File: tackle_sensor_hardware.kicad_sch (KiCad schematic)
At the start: 38 parts, among them J1 Conn_01x02_Male, J2 Conn_01x04_Male, J3 Conn_01x02_Male, Q1 DMP4051LK3, Q2 2N7002K, Q3 2N7002K, Q4 2N7002K, T1 DRQ125-330-R, U1 LIS2DE12, U2 STM32G031Fx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

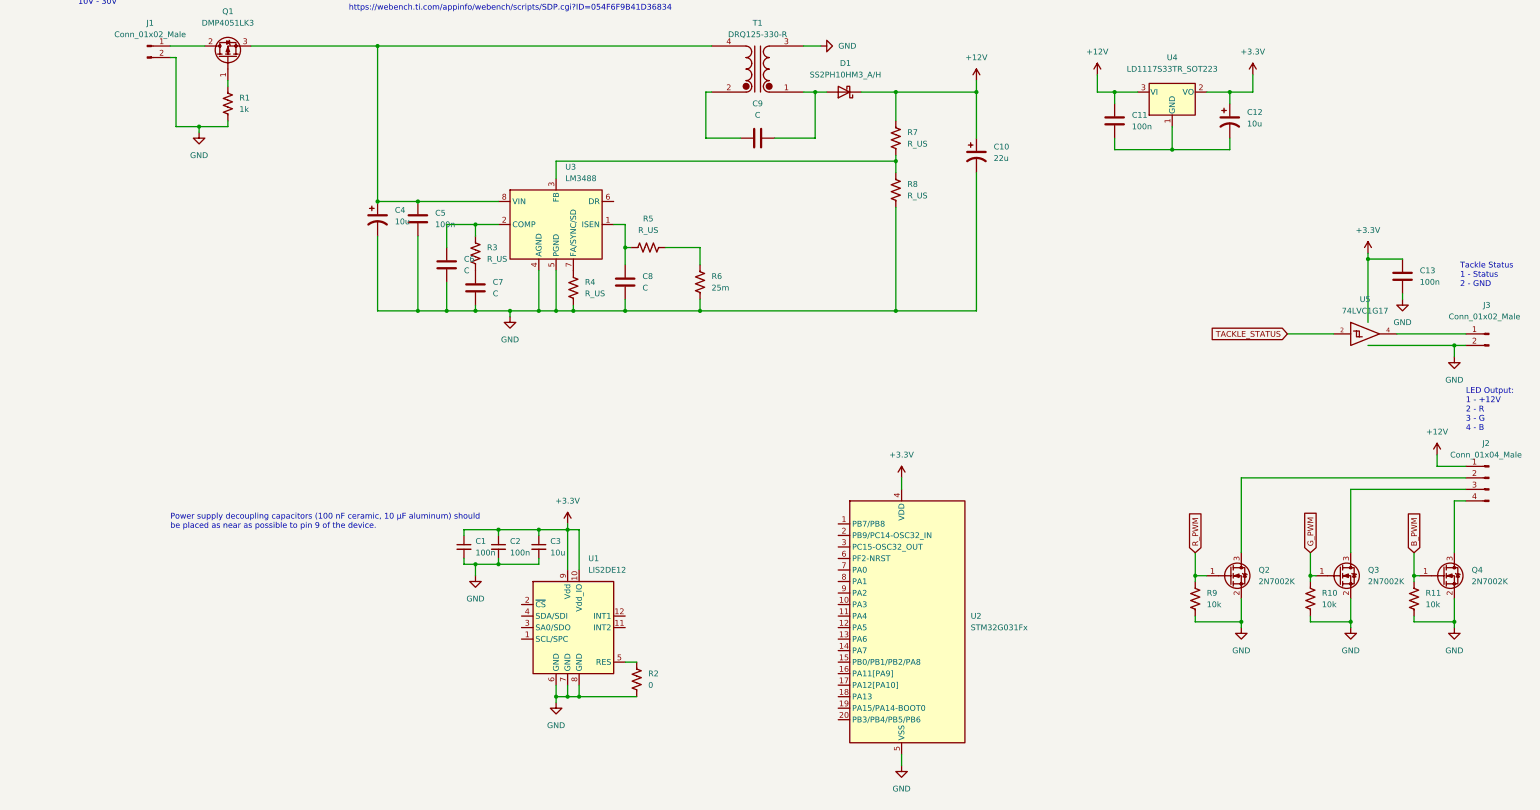
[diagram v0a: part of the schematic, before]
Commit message: (WIP) added prog header to schematic and added some WIP notes.
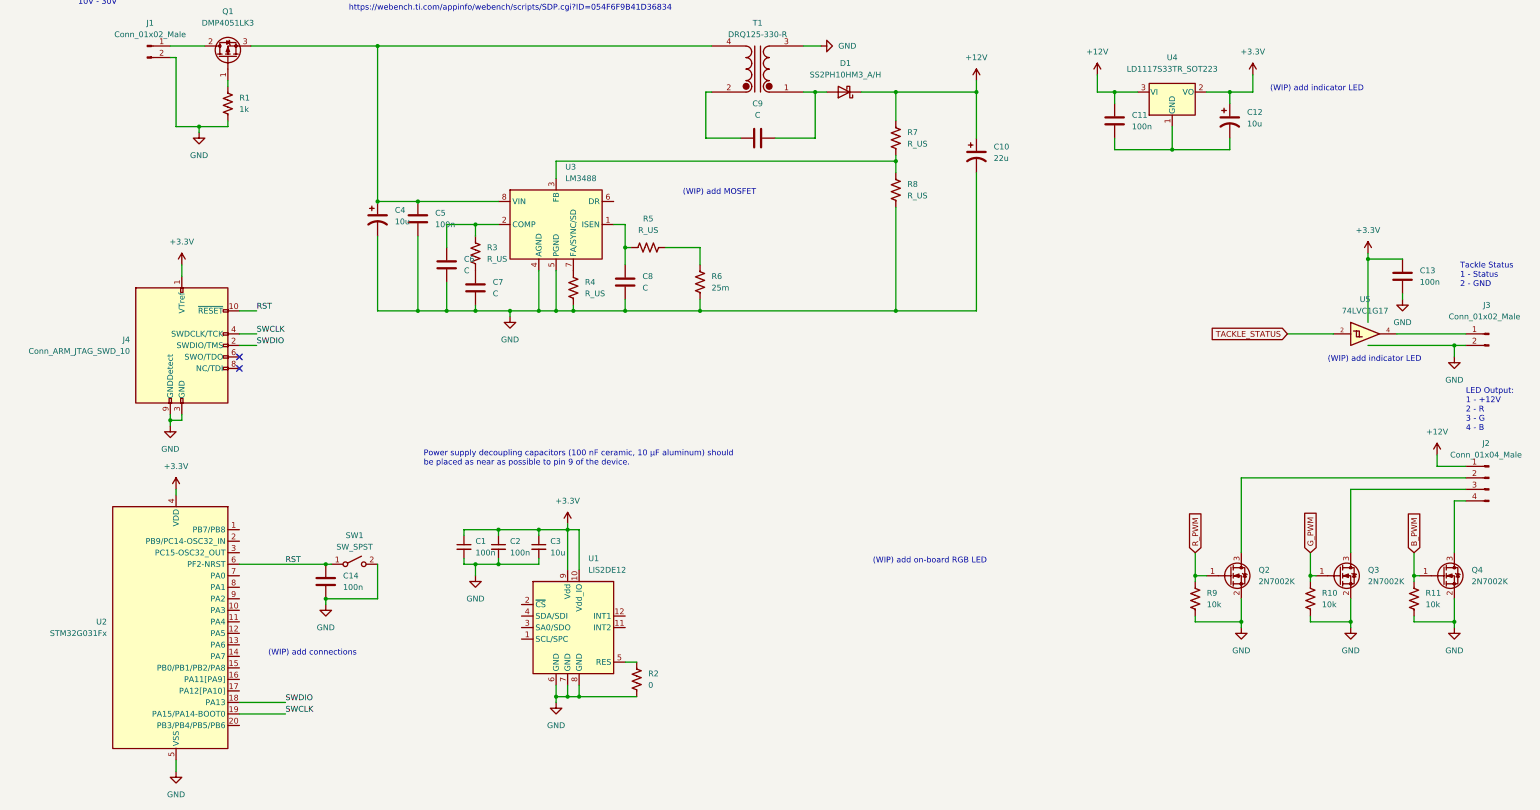
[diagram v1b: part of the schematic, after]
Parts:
- added C14: 100n, symbol Device:C
- added J4: Conn_ARM_JTAG_SWD_10, Connector_PinHeader_1.27mm:PinHeader_2x05_P1.27mm_Vertical, symbol Connector:Conn_ARM_JTAG_SWD_10
- added SW1: SW_SPST, symbol Switch:SW_SPST
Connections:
- net +3V3: now also J4.1 (VTref)
- net GND: now also C14.2, J4.3 (GND), J4.5 (GND), J4.9 (GNDDetect), SW1.2 (B)
- net SWDIO: now reaches U2.18 (PA13)
- net SWDIO: now also J4.2 (SWDIO/TMS)
- net SWCLK: now reaches U2.19 (PA15/PA14-BOOT0)
- net SWCLK: now also J4.4 (SWDCLK/TCK)
- net RST: now reaches U2.6 (PF2-NRST)
- net RST: now also C14.1, J4.10 (~{RESET}), SW1.1 (A)
- no-connect marks 0 -> 2
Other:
- note added: "(WIP) add MOSFET"
- note added: "(WIP) add connections"
- note added: "(WIP) add indicator LED"
- note added: "(WIP) add on-board RGB LED"
- moved on the sheet: U2

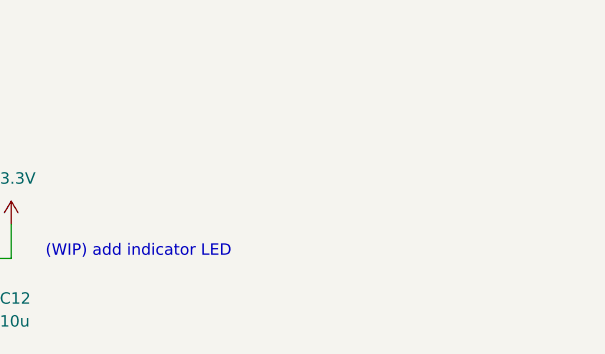
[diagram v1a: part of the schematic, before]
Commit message: added mounting holes
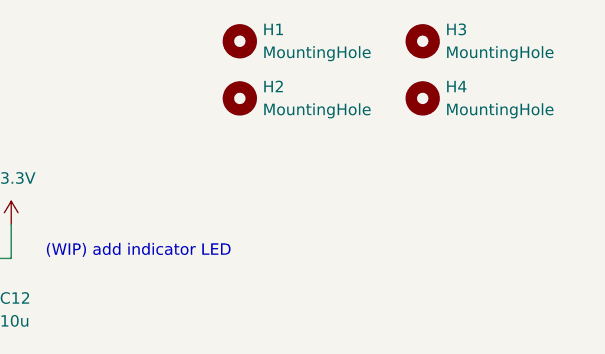
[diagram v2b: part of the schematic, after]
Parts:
- added H1, H2, H3, H4: MountingHole, MountingHole:MountingHole_3.2mm_M3, symbol Mechanical:MountingHole
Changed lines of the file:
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@@
     (pin "2")
+  )
+  (symbol (lib_id "Mechanical:MountingHole") (at 302.26 27.94 0) (unit 1)
+    (in_bom yes) (on_board yes) (fields_autoplaced)
+    (property "Reference" "H2" (id 0) (at 304.8 26.6699 0)
+      (effects (font (size 1.27 1.27)) (justify left))
+    )
+    (property "Value" "MountingHole" (id 1) (at 304.8 29.2099 0)
+      (effects (font (size 1.27 1.27)) (justify left))
+    )
+    (property "Footprint" "MountingHole:MountingHole_3.2mm_M3" (id 2) (at 302.26 27.94 0)
+      (effects (font (size 1.27 1.27)) hide)
+    )
+    (property "Datasheet" "~" (id 3) (at 302.26 27.94 0)
+      (effects (font (size 1.27 1.27)) hide)
+    )
   )
   (symbol (lib_id "Device:C") (at 105.41 88.9 0) (unit 1)
@@
     (pin "4")
   )
+  (symbol (lib_id "Mechanical:MountingHole") (at 322.58 21.59 0) (unit 1)
+    (in_bom yes) (on_board yes) (fields_autoplaced)
+    (property "Reference" "H3" (id 0) (at 325.12 20.3199 0)
+      (effects (font (size 1.27 1.27)) (justify left))
+    )
+    (property "Value" "MountingHole" (id 1) (at 325.12 22.8599 0)
+      (effects (font (size 1.27 1.27)) (justify left))
+    )
+    (property "Footprint" "MountingHole:MountingHole_3.2mm_M3" (id 2) (at 322.58 21.59 0)
+      (effects (font (size 1.27 1.27)) hide)
+    )
+    (property "Datasheet" "~" (id 3) (at 322.58 21.59 0)
+      (effects (font (size 1.27 1.27)) hide)
+    )
+  )
   (symbol (lib_id "Connector:Conn_ARM_JTAG_SWD_10") (at 40.64 101.6 0) (unit 1)
     (in_bom yes) (on_board yes) (fields_autoplaced)
@@
     (pin "2")
   )
+  (symbol (lib_id "Mechanical:MountingHole") (at 322.58 27.94 0) (unit 1)
+    (in_bom yes) (on_board yes) (fields_autoplaced)
+    (property "Reference" "H4" (id 0) (at 325.12 26.6699 0)
+      (effects (font (size 1.27 1.27)) (justify left))
+    )
+    (property "Value" "MountingHole" (id 1) (at 325.12 29.2099 0)
+      (effects (font (size 1.27 1.27)) (justify left))
+    )
+    (property "Footprint" "MountingHole:MountingHole_3.2mm_M3" (id 2) (at 322.58 27.94 0)
+      (effects (font (size 1.27 1.27)) hide)
+    )
+    (property "Datasheet" "~" (id 3) (at 322.58 27.94 0)
+      (effects (font (size 1.27 1.27)) hide)
+    )
+  )
+  (symbol (lib_id "Mechanical:MountingHole") (at 302.26 21.59 0) (unit 1)
+    (in_bom yes) (on_board yes) (fields_autoplaced)
+    (property "Reference" "H1" (id 0) (at 304.8 20.3199 0)
+      (effects (font (size 1.27 1.27)) (justify left))
+    )
+    (property "Value" "MountingHole" (id 1) (at 304.8 22.8599 0)
+      (effects (font (size 1.27 1.27)) (justify left))
+    )
+    (property "Footprint" "MountingHole:MountingHole_3.2mm_M3" (id 2) (at 302.26 21.59 0)
+      (effects (font (size 1.27 1.27)) hide)
+    )
+    (property "Datasheet" "~" (id 3) (at 302.26 21.59 0)
+      (effects (font (size 1.27 1.27)) hide)
+    )
+  )
   (symbol (lib_id "power:GND") (at 181.61 35.56 90) (unit 1)
     (in_bom yes) (on_board yes) (fields_autoplaced)
@@
       (reference "D1") (unit 1) (value "SS2PH10HM3_A/H") (footprint "")
     )
+    (path "/dff5c17e-362e-4954-b497-90231b41b9d7"
+      (reference "H1") (unit 1) (value "MountingHole") (footprint "MountingHole:MountingHole_3.2mm_M3")
+    )
+    (path "/42ddd32f-21c3-4d3d-b373-730648d1e4dd"
+      (reference "H2") (unit 1) (value "MountingHole") (footprint "MountingHole:MountingHole_3.2mm_M3")
+    )
+    (path "/90f6e54f-8e86-4885-a5e0-960086fd80b7"
+      (reference "H3") (unit 1) (value "MountingHole") (footprint "MountingHole:MountingHole_3.2mm_M3")
+    )
+    (path "/d0fd4895-a9a9-482b-81db-24fe34994515"
+      (reference "H4") (unit 1) (value "MountingHole") (footprint "MountingHole:MountingHole_3.2mm_M3")
+    )
     (path "/739b591f-ee89-4e4b-a089-6321966edc77"

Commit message: added on-board LEDs
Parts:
- removed SW1: SW_SPST, symbol Switch:SW_SPST
- added D2: CLV1A-FKB-CK1VW1DE1BB7C3C3, LED_SMD:LED_Cree-PLCC4_3.2x2.8mm_CCW, symbol rfc_symbol_lib:CLV1A-FKB-CK1VW1DE1BB7C3C3
- added D3, D?: LED, LED_SMD:LED_0603_1608Metric, symbol Device:LED
- added Q5, Q6, Q7: 2N7002K, Package_TO_SOT_SMD:SOT-23, symbol Transistor_FET:2N7002K
- added R12, R14, R16: 10k, Resistor_SMD:R_0603_1608Metric, symbol Device:R_US
- added R13, R15, R17, R18, R?: 1k, Resistor_SMD:R_0603_1608Metric, symbol Device:R_US
- added SW1: SW_Push, symbol Switch:SW_Push
- added SW2: SW_DIP_x01, Button_Switch_SMD:SW_DIP_SPSTx01_Slide_6.7x4.1mm_W8.61mm_P2.54mm_LowProfile, symbol Switch:SW_DIP_x01
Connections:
- net +12V: now also D2.2 (RK)
- net +3V3: now also D?.2 (A)
- net B_PWM: now also Q7.1 (G), R16.1
- net GND: now also Q5.2 (S), Q6.2 (S), Q7.2 (S), R12.2, R14.2, R16.2, R18.2, R?.2, SW1.2
- net G_PWM: now also Q6.1 (G), R14.1
- net RST: now also SW1.1
- net R_PWM: now also Q5.1 (G), R12.1
- net TACKLE_STATUS: now also D3.2 (A)
- new net: D3.1 (K), R18.1
- new net: Q7.3 (D), R17.2
- new net: D?.1 (K), R?.1
- new net: D2.1 (A), R13.1
- new net: D2.3 (GK), R17.1
- new net: D2.4 (BK), R15.1
- new net: Q5.3 (D), R13.2
- new net: Q6.3 (D), R15.2
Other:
- note added: "On-board RGB LED"
- note removed: "(WIP) add indicator LED"
- note removed: "(WIP) add on-board RGB LED"

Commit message: updated connectors, added 0 ohm resistors
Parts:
- removed C13: 100n, symbol Device:C
- removed D3: LED, LED_SMD:LED_0603_1608Metric, symbol Device:LED
- removed J3: Conn_01x02_Male, Connector_JST:JST_PH_B2B-PH-K_1x02_P2.00mm_Vertical, symbol Connector:Conn_01x02_Male
- removed U5: 74LVC1G17, Package_TO_SOT_SMD:SOT-353_SC-70-5, symbol 74xGxx:74LVC1G17
- added J3: Conn_01x03_Male, Connector_JST:JST_XH_B3B-XH-A_1x03_P2.50mm_Vertical, symbol Connector:Conn_01x03_Male
- added R20, R23: 0, Resistor_SMD:R_1210_3225Metric, symbol Device:R_US
- added R21, R22: 150, Resistor_SMD:R_0603_1608Metric, symbol Device:R_US
- J1: footprint Connector_PinHeader_2.54mm:PinHeader_1x02_P2.54mm_Vertical -> Connector_JST:JST_XH_B2B-XH-A_1x02_P2.50mm_Vertical
- J2: footprint Connector_JST:JST_PH_B4B-PH-K_1x04_P2.00mm_Vertical -> Connector_JST:JST_XH_B4B-XH-A_1x04_P2.50mm_Vertical
- R18: value 1k -> 0; footprint Resistor_SMD:R_0603_1608Metric -> Resistor_SMD:R_1210_3225Metric
- R4, R5, R6: footprint (none) -> Resistor_SMD:R_0603_1608Metric
- SW1, T1: footprint (none) -> Resistor_SMD:R_1210_3225Metric
- gave numbers to parts that had none: 2
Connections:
- net GND: now also J3.3 (Pin_3); no longer R18.2
- net TACKLE_STATUS: now also R21.1
- net at Q2.3 (D): now also R18.1; no longer J2.2 (Pin_2)
- net at Q4.3 (D): now also R23.1; no longer J2.4 (Pin_4)
- net at J2.3 (Pin_3): now also R20.2; no longer Q3.3 (D)
- new net: J3.1 (Pin_1), R22.2
- new net: J3.2 (Pin_2), R21.2
- new net: J2.4 (Pin_4), R23.2
- new net: J2.2 (Pin_2), R18.2
- new net: Q3.3 (D), R20.1
- new net UART_TX: R22.1
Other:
- note added: "Add Debug LED"
- note added: "Add UART TX output to this connector and stream the acceleration readings to the MCU plus the status 3 -pin connection"
- note added: "Add UART for Logging"
- note added: "Current Limit this output to 1A. PTC, Efuse. Potentially, add capability to shutoff this output. Add large 1210 0 ohm resistors to each of the LED channels"
- note added: "check for array or if these could be combined"

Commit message: added pinout to MCU
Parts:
- removed C14: 100n, symbol Device:C
- added C13: 100n, Capacitor_SMD:C_0603_1608Metric, symbol Device:C_Small
- added R24: 10k, Resistor_SMD:R_0603_1608Metric, symbol Device:R_US
- added TP1, TP10, TP11, TP2, TP3, TP4, TP5, TP6, TP7, TP8, TP9: TestPoint, symbol Connector:TestPoint
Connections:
- net +12V: now also TP10.1
- net +3V3: now also R24.1, TP11.1
- net B_PWM: now also U2.15 (PB0/PB1/PB2/PA8)
- net GND: now also C11.2, C12.2, SW2.2, U4.1 (GND), C13.2, TP1.1
- net G_PWM: now also U2.16 (PA11[PA9])
- net RST: now also C13.1, TP2.1
- net R_PWM: now also U2.20 (PB3/PB4/PB5/PB6)
- net TACKLE_STATUS: now also U2.2 (PB9/PC14-OSC32_IN)
- net UART_TX: now also U2.9 (PA2)
- net at C4.1, C5.1, Q1.3 (S)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: now also TP3.1
- net SPI1_SCK: now reaches U1.1 (SCL/SPC)
- net SPI1_SCK: now also U2.8 (PA1), TP7.1
- net ACC_INT2: now reaches U1.11 (INT2)
- net ACC_INT2: now also U2.12 (PA5), TP9.1
- net ACC_INT1: now reaches U1.12 (INT1)
- net ACC_INT1: now also U2.7 (PA0), TP8.1
- net SPI1_NSS: now reaches U1.2 (~{CS})
- net SPI1_NSS: now also U2.11 (PA4), TP4.1
- net SPI1_MISO: now reaches U1.3 (SA0/SDO)
- net SPI1_MISO: now also U2.13 (PA6), TP6.1
- net SPI1_MOSI: now reaches U1.4 (SDA/SDI)
- net SPI1_MOSI: now also U2.14 (PA7), TP5.1
- net UART_RX: now reaches U2.10 (PA3)
- net at U2.3 (PC15-OSC32_OUT): now also SW2.1, R24.2
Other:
- note added: "Add some diode protection here?"
- note added: "Mode Selection - Ineligible Receiver - Eligible Receiver"
- note removed: "(WIP) add connections"
- note removed: "Add Debug LED"
- note removed: "Add UART TX output to this connector and stream the acceleration readings to the MCU plus the status 3 -pin connection"
- note removed: "Add UART for Logging"
- note removed: "check for array or if these could be combined"
- moved on the sheet: C1, C2, C3, R2, SW1, SW2, U1

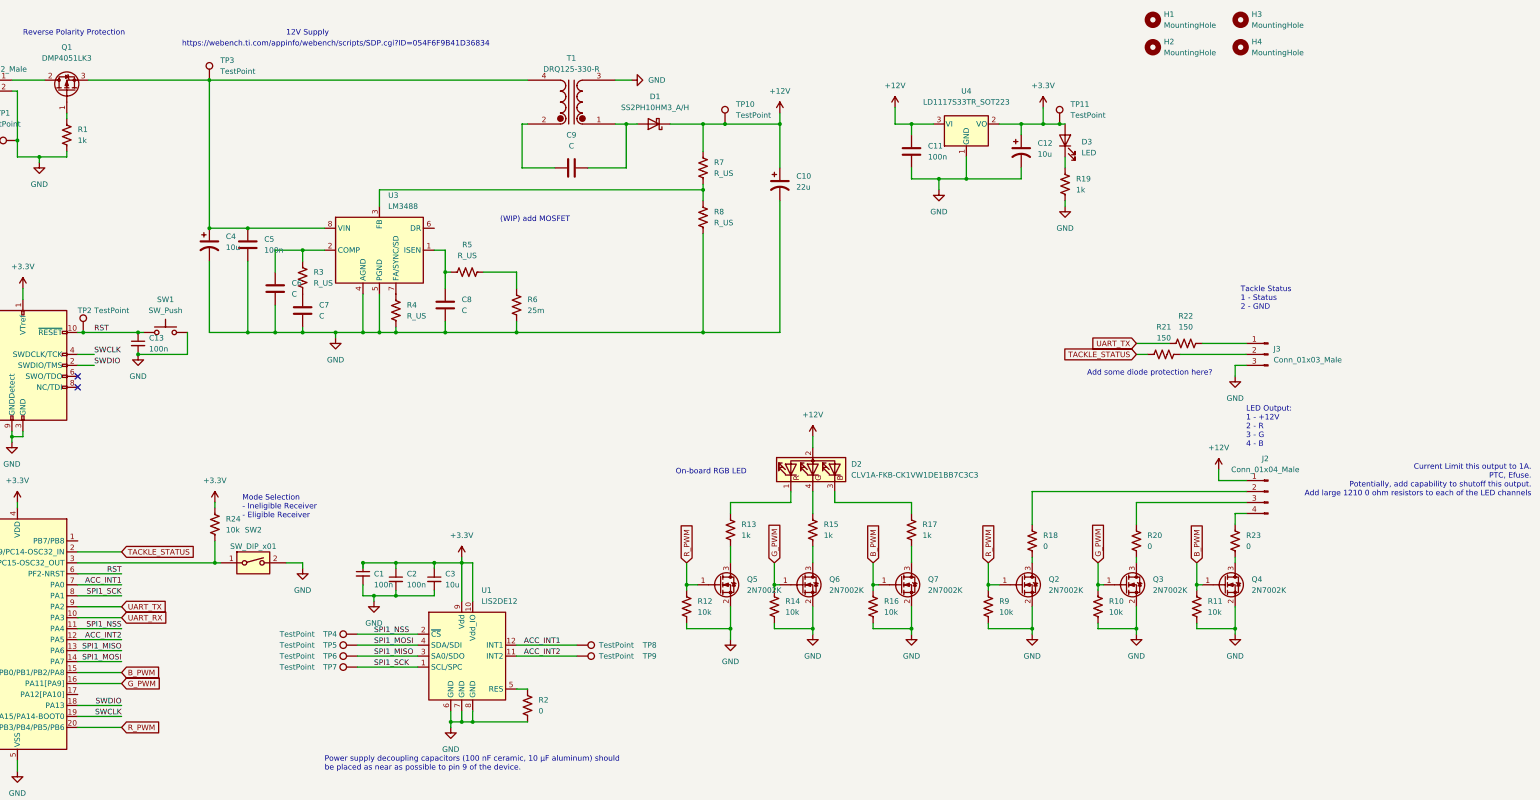
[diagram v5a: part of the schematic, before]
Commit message: added eFuse, added mosfet, added footprints
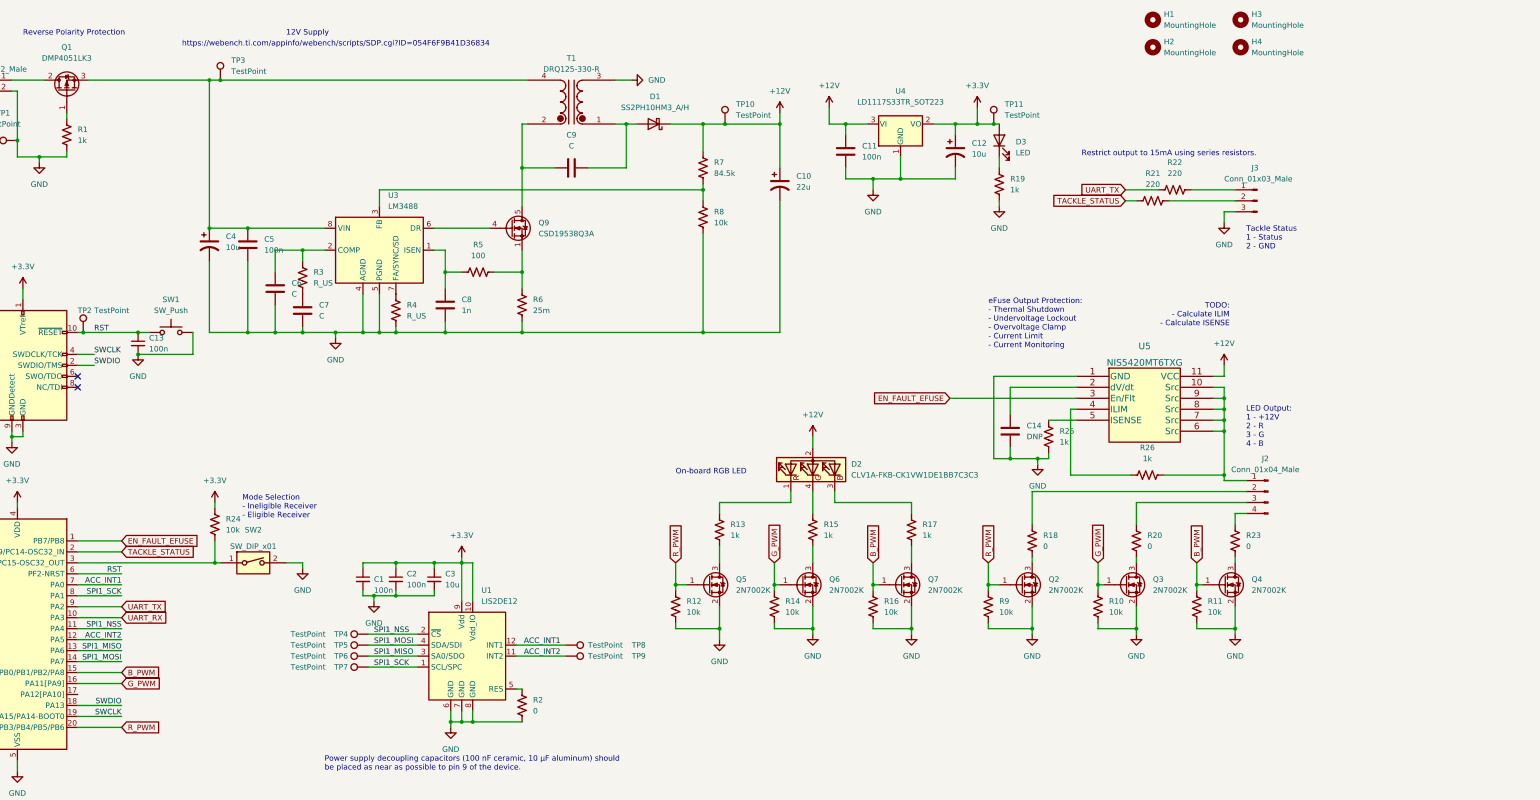
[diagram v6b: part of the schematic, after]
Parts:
- added C14: DNP, symbol Device:C
- added Q9: CSD19538Q3A, Package_SON:VSON-8_3.3x3.3mm_P0.65mm_NexFET, symbol rfc_symbol_lib:CSD19538Q3A
- added R25, R26: 1k, Resistor_SMD:R_0603_1608Metric, symbol Device:R_US
- added U5: NIS5420MT6TXG, rfc_footprint_lib:WDFN10_522AA-01_ONS, symbol rfc_symbol_lib:NIS5420MT6TXG
- C8: value C -> 1n
- R21, R22: value 150 -> 220
- R5: value R_US -> 100
- R7: value R_US -> 84.5k
- R8: value R_US -> 10k
- T1: footprint Resistor_SMD:R_1210_3225Metric -> rfc_footprint_lib:DRQ125-150-R
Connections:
- net +12V: now also U5.11 (VCC); no longer J2.1 (Pin_1)
- net GND: now also C14.2, R25.2, U5.1 (GND)
- net at U3.6 (DR): now also Q9.4 (G)
- net at R5.2, R6.1: now also Q9.1 (S), Q9.2 (S), Q9.3 (S)
- net at C9.2, T1.2 (AB): now also Q9.5 (D)
- net EN_FAULT_EFUSE: now reaches U2.1 (PB7/PB8)
- net EN_FAULT_EFUSE: now also U5.3 (En/Flt)
- new net: R26.1, U5.4 (ILIM)
- new net: J2.1 (Pin_1), R26.2, U5.10 (Src), U5.6 (Src), U5.7 (Src), U5.8 (Src), U5.9 (Src)
- new net: R25.1, U5.5 (ISENSE)
- new net: C14.1, U5.2 (dV/dt)
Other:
- note added: "Restrict output to 15mA using series resistors."
- note added: "TODO: - Calculate ILIM - Calculate ISENSE"
- note added: "eFuse Output Protection: - Thermal Shutdown - Undervoltage Lockout - Overvoltage Clamp - Current Limit - Current Monitoring"
- note removed: "(WIP) add MOSFET"
- note removed: "Add some diode protection here?"
- note removed: "Current Limit this output to 1A. PTC, Efuse. Potentially, add capability to shutoff this output. Add large 1210 0 ohm resistors to each of the LED channels"
- moved on the sheet: C1, C11, C12, D3, J3, Q5, R12, R13, R19, R2, R21, R22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
